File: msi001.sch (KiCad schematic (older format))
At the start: 33 parts, among them J1 SMA_UHF, J2 Raspberry_Pi_2_3, U2 B39431B3710U410, U3 msi001, U6 PGA-103

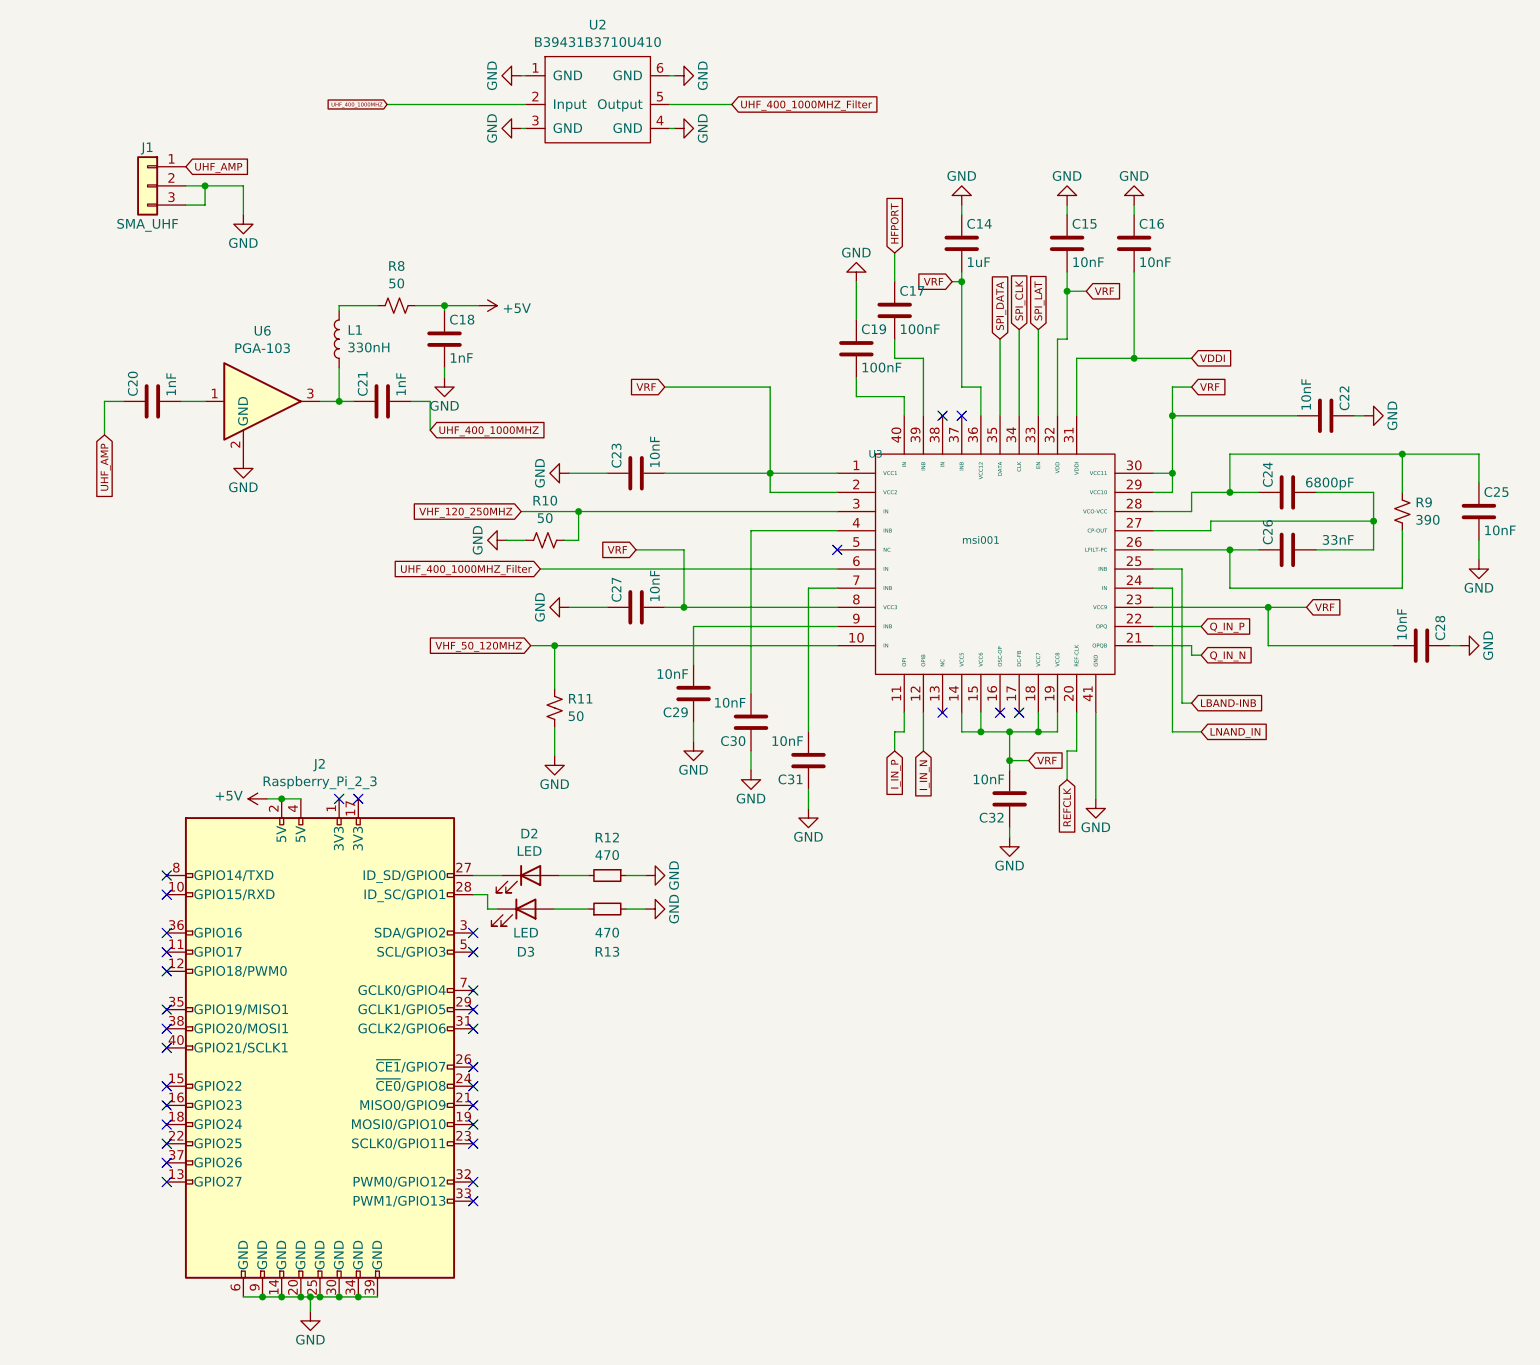
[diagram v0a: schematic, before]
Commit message: adding v2 2 filter front end filter
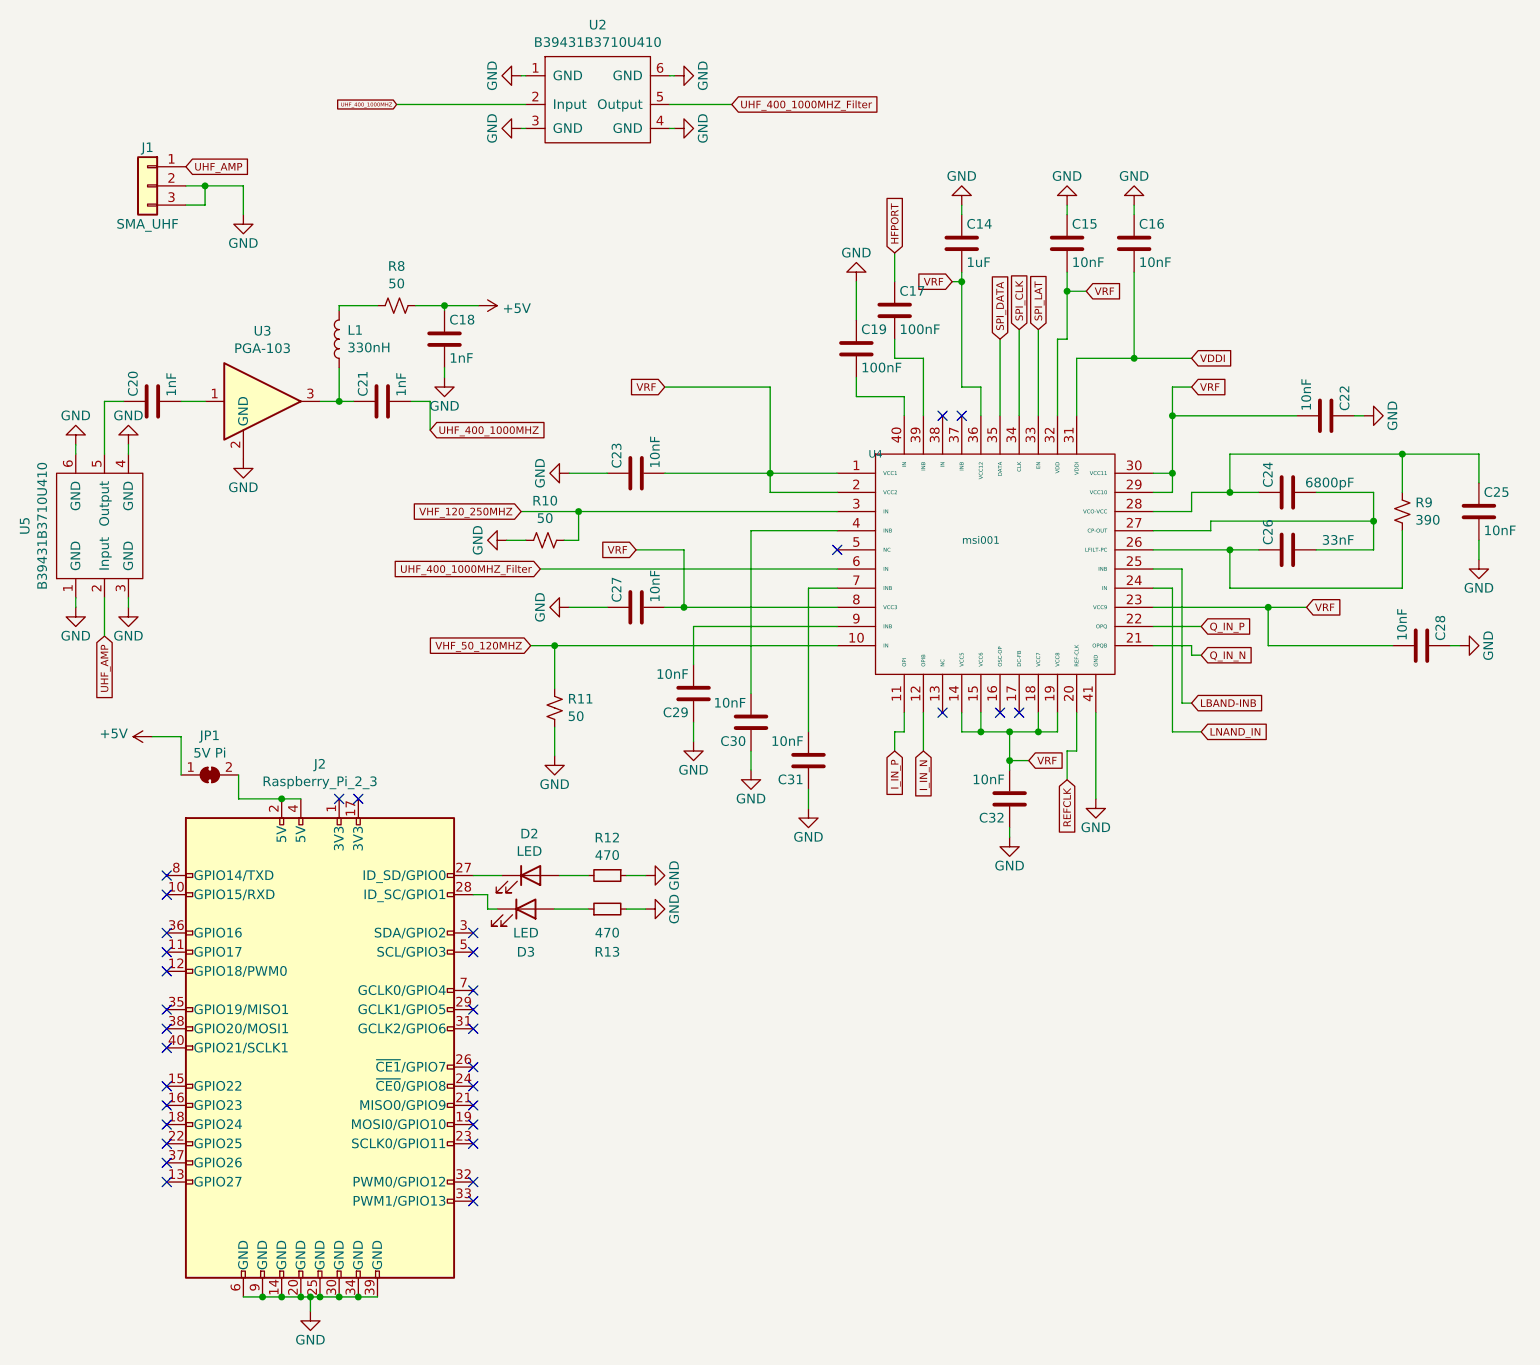
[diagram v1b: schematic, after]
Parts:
- added JP1: 5V Pi, Jumper:SolderJumper-2_P1.3mm_Bridged_RoundedPad1.0x1.5mm, symbol Jumper:SolderJumper_2_Bridged
- added U5: B39431B3710U410, Package_DFN_QFN:DFN-6-1EP_3x3mm_P1mm_EP1.5x2.4mm, symbol SAW_filter_6pin:B39431B3710U410
- renumbered U6 to U3, U3 to U4
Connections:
- net +5V: now also JP1.1 (A); no longer J2.2 (5V), J2.4 (5V)
- net GND: now also U5.1 (GND), U5.3 (GND), U5.4 (GND), U5.6 (GND)
- net UHF_AMP: now also U5.2 (Input); no longer C20.1
- new net: J2.2 (5V), J2.4 (5V), JP1.2 (B)
- new net: C20.1, U5.5 (Output)
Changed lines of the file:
@@
 encoding utf-8
 Sheet 3 5
-Title ""
+Title "AfriCUBE Satellite"
 Date ""
-Rev ""
-Comp ""
-Comment1 ""
+Rev "Version 1.0"
+Comp "GigaTechnology / AMSATSA"
+Comment1 "Anton Janovsky  Shahn Pretorius"
 Comment2 ""
 Comment3 ""
@@
 $EndDescr
 $Comp
-L power:GND #PWR032
+L power:GND #PWR034
 U 1 1 5C68EDE0
 P 3300 3100
-F 0 "#PWR032" H 3300 2850 50  0001 C CNN
+F 0 "#PWR034" H 3300 2850 50  0001 C CNN
 F 1 "GND" H 3300 2950 50  0000 C CNN
 F 2 "" H 3300 3100 50  0001 C CNN
@@
 $EndComp
 $Comp
-L power:GND #PWR029
+L power:GND #PWR030
 U 1 1 5C68F768
 P 7450 2800
-F 0 "#PWR029" H 7450 2550 50  0001 C CNN
+F 0 "#PWR030" H 7450 2550 50  0001 C CNN
 F 1 "GND" H 7450 2650 50  0000 C CNN
 F 2 "" H 7450 2800 50  0001 C CNN
@@
 Connection ~ 7650 3000
 $Comp
-L power:GND #PWR034
+L power:GND #PWR036
 U 1 1 5C68FE9A
 P 8050 3550
-F 0 "#PWR034" H 8050 3300 50  0001 C CNN
+F 0 "#PWR036" H 8050 3300 50  0001 C CNN
 F 1 "GND" H 8050 3400 50  0000 C CNN
 F 2 "" H 8050 3550 50  0001 C CNN
@@
 $EndComp
 $Comp
-L power:GND #PWR036
+L power:GND #PWR040
 U 1 1 5C69029B
 P 7950 4000
-F 0 "#PWR036" H 7950 3750 50  0001 C CNN
+F 0 "#PWR040" H 7950 3750 50  0001 C CNN
 F 1 "GND" H 7950 3850 50  0000 C CNN
 F 2 "" H 7950 4000 50  0001 C CNN
@@
 Connection ~ 6950 3800
 $Comp
-L power:GND #PWR041
+L power:GND #PWR045
 U 1 1 5C69072D
 P 6050 4800
-F 0 "#PWR041" H 6050 4550 50  0001 C CNN
+F 0 "#PWR045" H 6050 4550 50  0001 C CNN
 F 1 "GND" H 6050 4650 50  0000 C CNN
 F 2 "" H 6050 4800 50  0001 C CNN
@@
 $EndComp
 $Comp
-L power:GND #PWR043
+L power:GND #PWR047
 U 1 1 5C690DC7
 P 5600 5000
-F 0 "#PWR043" H 5600 4750 50  0001 C CNN
+F 0 "#PWR047" H 5600 4750 50  0001 C CNN
 F 1 "GND" H 5600 4850 50  0000 C CNN
 F 2 "" H 5600 5000 50  0001 C CNN
@@
 NoConn ~ 5250 4350
 $Comp
-L power:GND #PWR035
+L power:GND #PWR039
 U 1 1 5C6913B6
 P 3300 3800
-F 0 "#PWR035" H 3300 3550 50  0001 C CNN
+F 0 "#PWR039" H 3300 3550 50  0001 C CNN
 F 1 "GND" H 3300 3650 50  0000 C CNN
 F 2 "" H 3300 3800 50  0001 C CNN
@@
 Connection ~ 3900 3800
 $Comp
-L power:GND #PWR037
+L power:GND #PWR042
 U 1 1 5C69151F
 P 3950 4500
-F 0 "#PWR037" H 3950 4250 50  0001 C CNN
+F 0 "#PWR042" H 3950 4250 50  0001 C CNN
 F 1 "GND" H 3950 4350 50  0000 C CNN
 F 2 "" H 3950 4500 50  0001 C CNN
@@
 	3950 4400 3950 4500
 $Comp
-L power:GND #PWR039
+L power:GND #PWR044
 U 1 1 5C69180E
 P 4250 4650
-F 0 "#PWR039" H 4250 4400 50  0001 C CNN
+F 0 "#PWR044" H 4250 4400 50  0001 C CNN
 F 1 "GND" H 4250 4500 50  0000 C CNN
 F 2 "" H 4250 4650 50  0001 C CNN
@@
 	4700 3400 4250 3400
 $Comp
-L power:GND #PWR042
+L power:GND #PWR046
 U 1 1 5C69199F
 P 4550 4850
-F 0 "#PWR042" H 4550 4600 50  0001 C CNN
+F 0 "#PWR046" H 4550 4600 50  0001 C CNN
 F 1 "GND" H 4550 4700 50  0000 C CNN
 F 2 "" H 4550 4850 50  0001 C CNN
@@
 	6450 3700 6350 3700
 $Comp
-L msi001:msi001 U3
+L msi001:msi001 U4
 U 1 1 5C698FED
 P 4900 3000
-F 0 "U3" H 4900 3000 39  0000 C CNN
+F 0 "U4" H 4900 3000 39  0000 C CNN
 F 1 "msi001" H 5450 2550 39  0000 C CNN
 F 2 "Package_DFN_QFN:QFN-40-1EP_6x6mm_P0.5mm_EP4.6x4.6mm" H 4900 3000 39  0001 C CNN
@@
 Wire Wire Line
 	5600 4600 5600 4450
-Text GLabel 2350 1175 0    20   Input ~ 0
+Text GLabel 2400 1175 0    20   Input ~ 0
 UHF_400_1000MHZ
 $Comp
@@
 $EndComp
 Wire Wire Line
-	2350 1175 3075 1175
-Wire Wire Line
 	3825 1175 4150 1175
 Wire Wire Line
@@
 $EndComp
 $Comp
-L power:GND #PWR033
+L power:GND #PWR035
 U 1 1 60159695
 P 2975 3450
-F 0 "#PWR033" H 2975 3200 50  0001 C CNN
+F 0 "#PWR035" H 2975 3200 50  0001 C CNN
 F 1 "GND" H 2975 3300 50  0000 C CNN
 F 2 "" H 2975 3450 50  0001 C CNN
@@
 $EndComp
 $Comp
-L power:GND #PWR038
+L power:GND #PWR043
 U 1 1 60159A6B
 P 3225 4575
-F 0 "#PWR038" H 3225 4325 50  0001 C CNN
+F 0 "#PWR043" H 3225 4325 50  0001 C CNN
 F 1 "GND" H 3225 4425 50  0000 C CNN
 F 2 "" H 3225 4575 50  0001 C CNN
@@
 	1950 7400 2000 7400
 $Comp
-L power:GND #PWR046
+L power:GND #PWR050
 U 1 1 6016A670
 P 1950 7475
-F 0 "#PWR046" H 1950 7225 50  0001 C CNN
+F 0 "#PWR050" H 1950 7225 50  0001 C CNN
 F 1 "GND" H 1950 7325 50  0000 C CNN
 F 2 "" H 1950 7475 50  0001 C CNN
@@
 Wire Wire Line
 	1800 4800 1900 4800
-Wire Wire Line
-	1725 4800 1800 4800
-$Comp
-L power:+5V #PWR040
+$Comp
+L power:+5V #PWR041
 U 1 1 601FD54B
-P 1725 4800
-F 0 "#PWR040" H 1725 4650 50  0001 C CNN
-F 1 "+5V" V 1740 4928 50  0000 L CNN
-F 2 "" H 1725 4800 50  0001 C CNN
-F 3 "" H 1725 4800 50  0001 C CNN
-	1    1725 4800
+P 1125 4475
+F 0 "#PWR041" H 1125 4325 50  0001 C CNN
+F 1 "+5V" V 1140 4603 50  0000 L CNN
+F 2 "" H 1125 4475 50  0001 C CNN
+F 3 "" H 1125 4475 50  0001 C CNN
+	1    1125 4475
 	0    -1   -1   0
 $EndComp
@@
 	3600 5375 3700 5375
 $Comp
-L power:GND #PWR044
+L power:GND #PWR048
 U 1 1 602F39AF
 P 3700 5200
-F 0 "#PWR044" H 3700 4950 50  0001 C CNN
+F 0 "#PWR048" H 3700 4950 50  0001 C CNN
 F 1 "GND" H 3700 5050 50  0000 C CNN
 F 2 "" H 3700 5200 50  0001 C CNN
@@
 $EndComp
 $Comp
-L power:GND #PWR045
+L power:GND #PWR049
 U 1 1 602F3F63
 P 3700 5375
-F 0 "#PWR045" H 3700 5125 50  0001 C CNN
+F 0 "#PWR049" H 3700 5125 50  0001 C CNN
 F 1 "GND" H 3700 5225 50  0000 C CNN
 F 2 "" H 3700 5375 50  0001 C CNN
@@
 Connection ~ 2650 2225
 Wire Wire Line
-	875  2725 875  2900
-Wire Wire Line
 	875  2725 975  2725
 $Comp
-L power:GND #PWR031
+L power:GND #PWR033
 U 1 1 60205A61
 P 1600 3025
-F 0 "#PWR031" H 1600 2775 50  0001 C CNN
+F 0 "#PWR033" H 1600 2775 50  0001 C CNN
 F 1 "GND" H 1600 2875 50  0000 C CNN
 F 2 "" H 1600 3025 50  0001 C CNN
@@
 $EndComp
 $Comp
-L power:GND #PWR0101
+L power:GND #PWR029
 U 1 1 60206B95
 P 2650 2600
-F 0 "#PWR0101" H 2650 2350 50  0001 C CNN
+F 0 "#PWR029" H 2650 2350 50  0001 C CNN
 F 1 "GND" H 2650 2450 50  0000 C CNN
 F 2 "" H 2650 2600 50  0001 C CNN
@@
 Text GLabel 1300 1500 2    39   Input ~ 0
 UHF_AMP
-Text GLabel 875  2900 3    39   Input ~ 0
+Text GLabel 875  3950 3    39   Input ~ 0
 UHF_AMP
 Wire Wire Line
@@
 UHF_400_1000MHZ_Filter
 $Comp
-L RF_Amplifier:PGA-103 U6
+L RF_Amplifier:PGA-103 U3
 U 1 1 6020BAAF
 P 1700 2725
-F 0 "U6" H 1700 3092 50  0000 C CNN
+F 0 "U3" H 1700 3092 50  0000 C CNN
 F 1 "PGA-103" H 1700 3001 50  0000 C CNN
 F 2 "Package_TO_SOT_SMD:SOT-89-3" H 1750 3125 50  0001 C CNN
@@
 $EndComp
 $Comp
-L power:+5V #PWR0102
+L power:+5V #PWR028
 U 1 1 60211024
 P 2825 2225
-F 0 "#PWR0102" H 2825 2075 50  0001 C CNN
+F 0 "#PWR028" H 2825 2075 50  0001 C CNN
 F 1 "+5V" V 2840 2353 50  0000 L CNN
 F 2 "" H 2825 2225 50  0001 C CNN
@@
 	0    1    1    0
 $EndComp
+$Comp
+L Jumper:SolderJumper_2_Bridged JP1
+U 1 1 6025AAC9
+P 1425 4675
+F 0 "JP1" H 1425 4880 50  0000 C CNN
+F 1 "5V Pi" H 1425 4789 50  0000 C CNN
+F 2 "Jumper:SolderJumper-2_P1.3mm_Bridged_RoundedPad1.0x1.5mm" H 1425 4675 50  0001 C CNN
+F 3 "~" H 1425 4675 50  0001 C CNN
+	1    1425 4675
+	1    0    0    -1
+$EndComp
+Wire Wire Line
+	1125 4475 1275 4475
+Wire Wire Line
+	1275 4475 1275 4675
+Wire Wire Line
+	1575 4800 1800 4800
+Wire Wire Line
+	1575 4675 1575 4800
+$Comp
+L SAW_filter_6pin:B39431B3710U410 U?
+U 1 1 603CC4FD
+P 875 3375
+AR Path="/5C68CE5E/603CC4FD" Ref="U?"  Part="1"
+AR Path="/5C68CE4D/603CC4FD" Ref="U5"  Part="1"
+F 0 "U5" H 875 3790 50  0000 C CNN
+F 1 "B39431B3710U410" H 875 3699 50  0000 C CNN
+F 2 "Package_DFN_QFN:DFN-6-1EP_3x3mm_P1mm_EP1.5x2.4mm" H 975 3175 50  0001 C CNN
+F 3 "" H 975 3175 50  0001 C CNN
+	1    875  3375
+	0    -1   -1   0
+$EndComp
+Wire Wire Line
+	1000 3800 1000 3750
+Wire Wire Line
+	725  3800 725  3750
+Wire Wire Line
+	725  3000 725  2950
+Wire Wire Line
+	1000 2950 1000 3000
+$Comp
+L power:GND #PWR?
+U 1 1 60408688
+P 725 3800
+AR Path="/5C68CE5E/60408688" Ref="#PWR?"  Part="1"
+AR Path="/5C68CE4D/60408688" Ref="#PWR037"  Part="1"
+F 0 "#PWR037" H 725 3550 50  0001 C CNN
+F 1 "GND" H 725 3650 50  0000 C CNN
+F 2 "" H 725 3800 50  0001 C CNN
+F 3 "" H 725 3800 50  0001 C CNN
+	1    725  3800
+	1    0    0    -1
+$EndComp
+$Comp
+L power:GND #PWR?
+U 1 1 60408AF4
+P 1000 3800
+AR Path="/5C68CE5E/60408AF4" Ref="#PWR?"  Part="1"
+AR Path="/5C68CE4D/60408AF4" Ref="#PWR038"  Part="1"
+F 0 "#PWR038" H 1000 3550 50  0001 C CNN
+F 1 "GND" H 1000 3650 50  0000 C CNN
+F 2 "" H 1000 3800 50  0001 C CNN
+F 3 "" H 1000 3800 50  0001 C CNN
+	1    1000 3800
+	1    0    0    -1
+$EndComp
+$Comp
+L power:GND #PWR?
+U 1 1 604091EA
+P 725 2950
+AR Path="/5C68CE5E/604091EA" Ref="#PWR?"  Part="1"
+AR Path="/5C68CE4D/604091EA" Ref="#PWR031"  Part="1"
+F 0 "#PWR031" H 725 2700 50  0001 C CNN
+F 1 "GND" H 725 2800 50  0000 C CNN
+F 2 "" H 725 2950 50  0001 C CNN
+F 3 "" H 725 2950 50  0001 C CNN
+	1    725  2950
+	-1   0    0    1
+$EndComp
+$Comp
+L power:GND #PWR?
+U 1 1 60409720
+P 1000 2950
+AR Path="/5C68CE5E/60409720" Ref="#PWR?"  Part="1"
+AR Path="/5C68CE4D/60409720" Ref="#PWR032"  Part="1"
+F 0 "#PWR032" H 1000 2700 50  0001 C CNN
+F 1 "GND" H 1000 2800 50  0000 C CNN
+F 2 "" H 1000 2950 50  0001 C CNN
+F 3 "" H 1000 2950 50  0001 C CNN
+	1    1000 2950
+	-1   0    0    1
+$EndComp
+Wire Wire Line
+	875  3750 875  3950
+Wire Wire Line
+	875  3000 875  2725
+Wire Wire Line
+	3075 1175 2400 1175
 $EndSCHEMATC
